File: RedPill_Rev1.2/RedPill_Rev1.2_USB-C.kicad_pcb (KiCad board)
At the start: 2 copper layers, 21.6 x 66 mm, 26 parts, among them J1 Conn_01x04, J2 Conn_01x04, J3 USB_B_Mini, J5 Pin_01x20, J6 Pin_01x20, SW1 SW_Push, U1 TLV1117-33, U2 STM32G0B1KET6, X1 SG-5032CAN

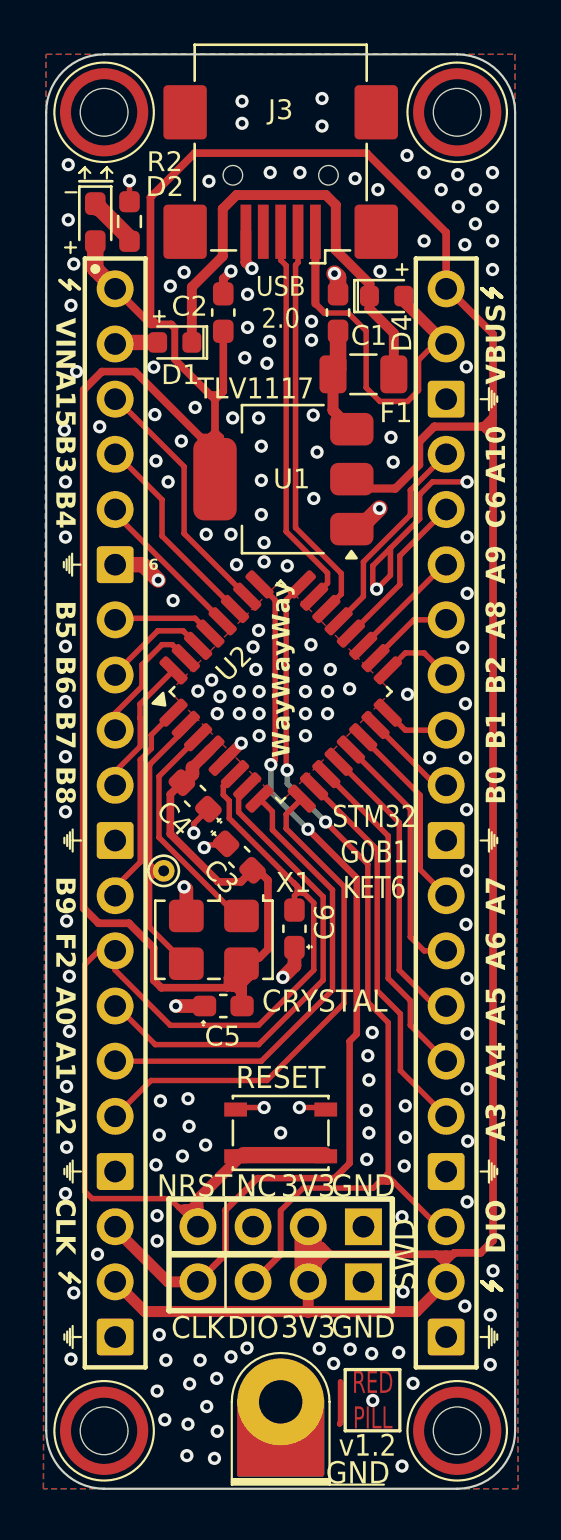
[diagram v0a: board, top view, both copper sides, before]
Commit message: Added USB-C
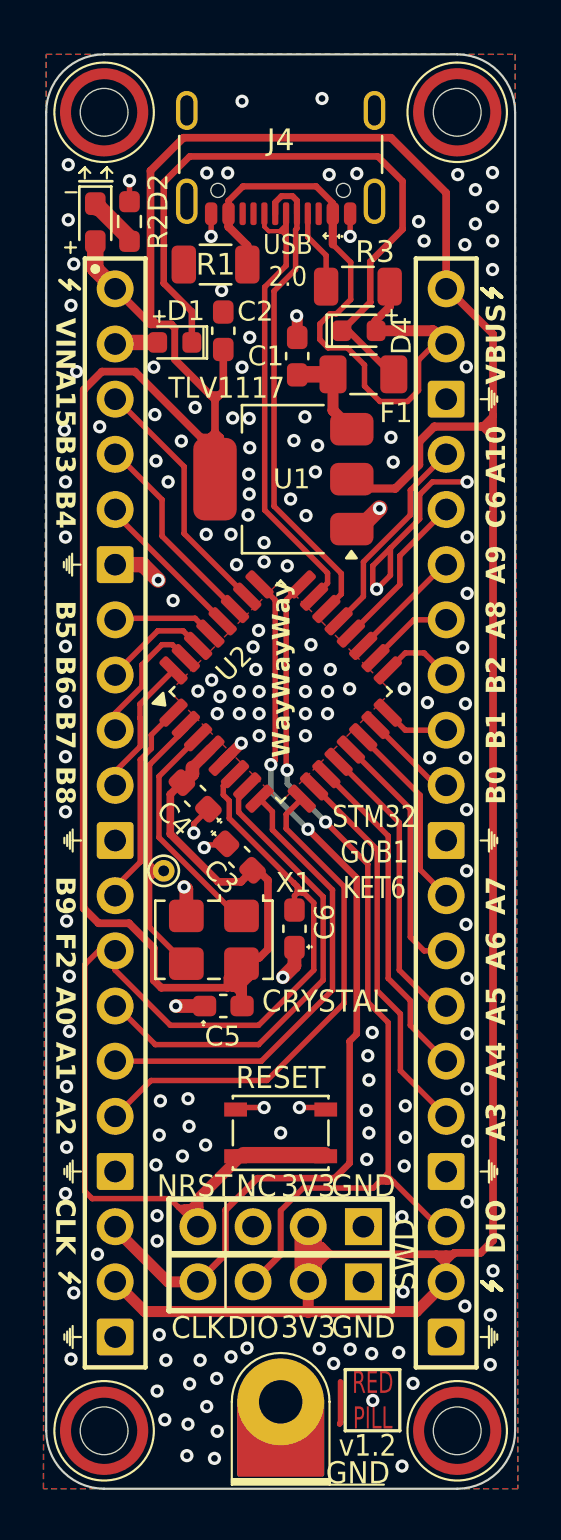
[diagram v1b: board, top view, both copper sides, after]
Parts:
- removed J3: USB_B_Mini, Connector_USB:USB_Mini-B_Wuerth_65100516121_Horizontal
- added J4: USB_C_Receptacle_USB2.0_16P, Connector_USB:USB_C_Receptacle_GCT_USB4105-xx-A_16P_TopMnt_Horizontal, F.Cu at (100.6, 33.4)
- added R1: 56k, Resistor_SMD:R_1206_3216Metric, F.Cu at (97.6, 39.4)
- added R3: 56k, Resistor_SMD:R_1206_3216Metric, F.Cu at (104.2, 40.4)
- F1: value Polyfuse_Small -> Polyfuse
- H1: value MountingHole -> M2_2.2mm_TL
- H2: value MountingHole -> M2_2.2mm_TR
- H3: value MountingHole -> M2_2.2mm_BL
- H4: value MountingHole -> M2_2.2mm_BR
- J1, J2: value Conn_01x04 -> Pin_01x04
- SW1: value SW_Push -> PTS810
- TP5: value TestPoint -> GND Test
- moved C1 2.75 mm to (101.4, 43.6)
- moved D4 2.04 mm to (104.2, 42.4)
- moved C2 0.84 mm to (98.0, 42.4)
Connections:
- net /REG_IN renamed /DIODE_VOUT
- J5 pad 18: /SYS_SWCLK -> /SWCLK
- U2 pad 24: /SYS_SWDIO -> /SWDIO
- U2 pad 25: /SYS_SWCLK -> /SWCLK
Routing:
- net VBUS: track 17.7 -> 31.4 mm
- net /DIODE_VOUT: track 21.5 -> 31.6 mm
- net Net-(J4-CC1): track 0.00 -> 4.37 mm
- net /USB_D+: track 18.0 -> 22.2 mm
- net /USB_D-: track 18.6 -> 22.5 mm
- net +3V3: track 197.5 -> 199.4 mm
- net GND: track 31.2 -> 30.3 mm, vias 177 -> 170

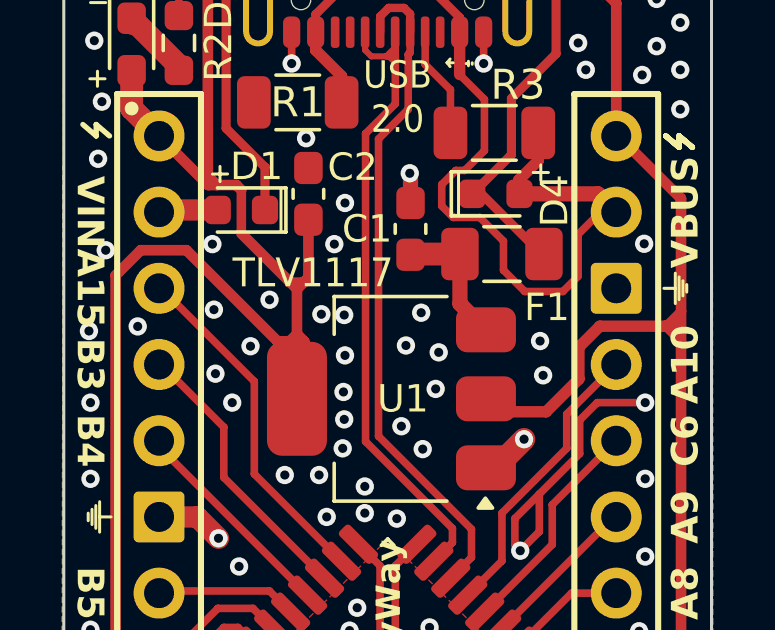
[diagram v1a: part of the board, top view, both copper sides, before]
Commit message: Made silkscreen pretty
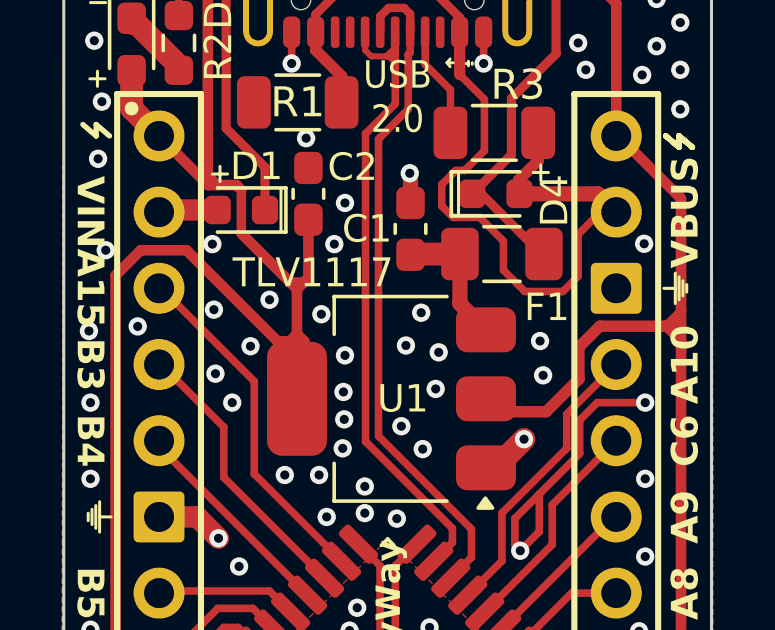
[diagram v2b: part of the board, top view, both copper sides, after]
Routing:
- net GND: vias 170 -> 169
